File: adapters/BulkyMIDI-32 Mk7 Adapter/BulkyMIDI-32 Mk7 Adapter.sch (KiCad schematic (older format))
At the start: 12 parts, among them J1 Gameport, J2 MIDI OUT, J3 MIDI IN, U1 6N138, U3 74LS00

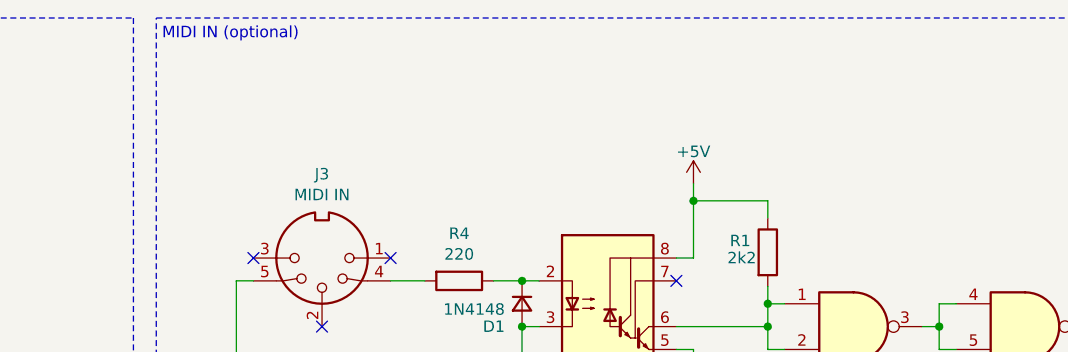
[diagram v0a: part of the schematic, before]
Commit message: Add schematic
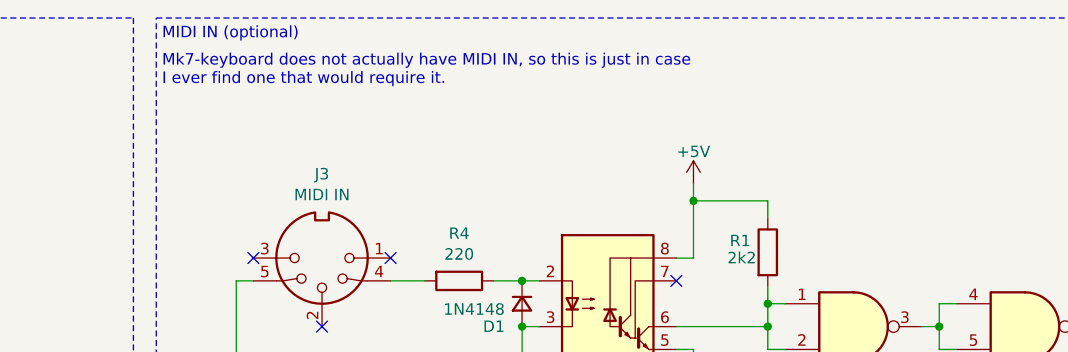
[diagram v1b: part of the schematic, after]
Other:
- note added: "Mk7-keyboard does not actually have MIDI IN, so this is just in case\nI ever find one that would require it."
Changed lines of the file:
@@
 Text Notes 1925 1250 0    50   ~ 0
 Gameport
+Text Notes 5125 1450 0    50   ~ 0
+Mk7-keyboard does not actually have MIDI IN, so this is just in case\nI ever find one that would require it.
 $EndSCHEMATC

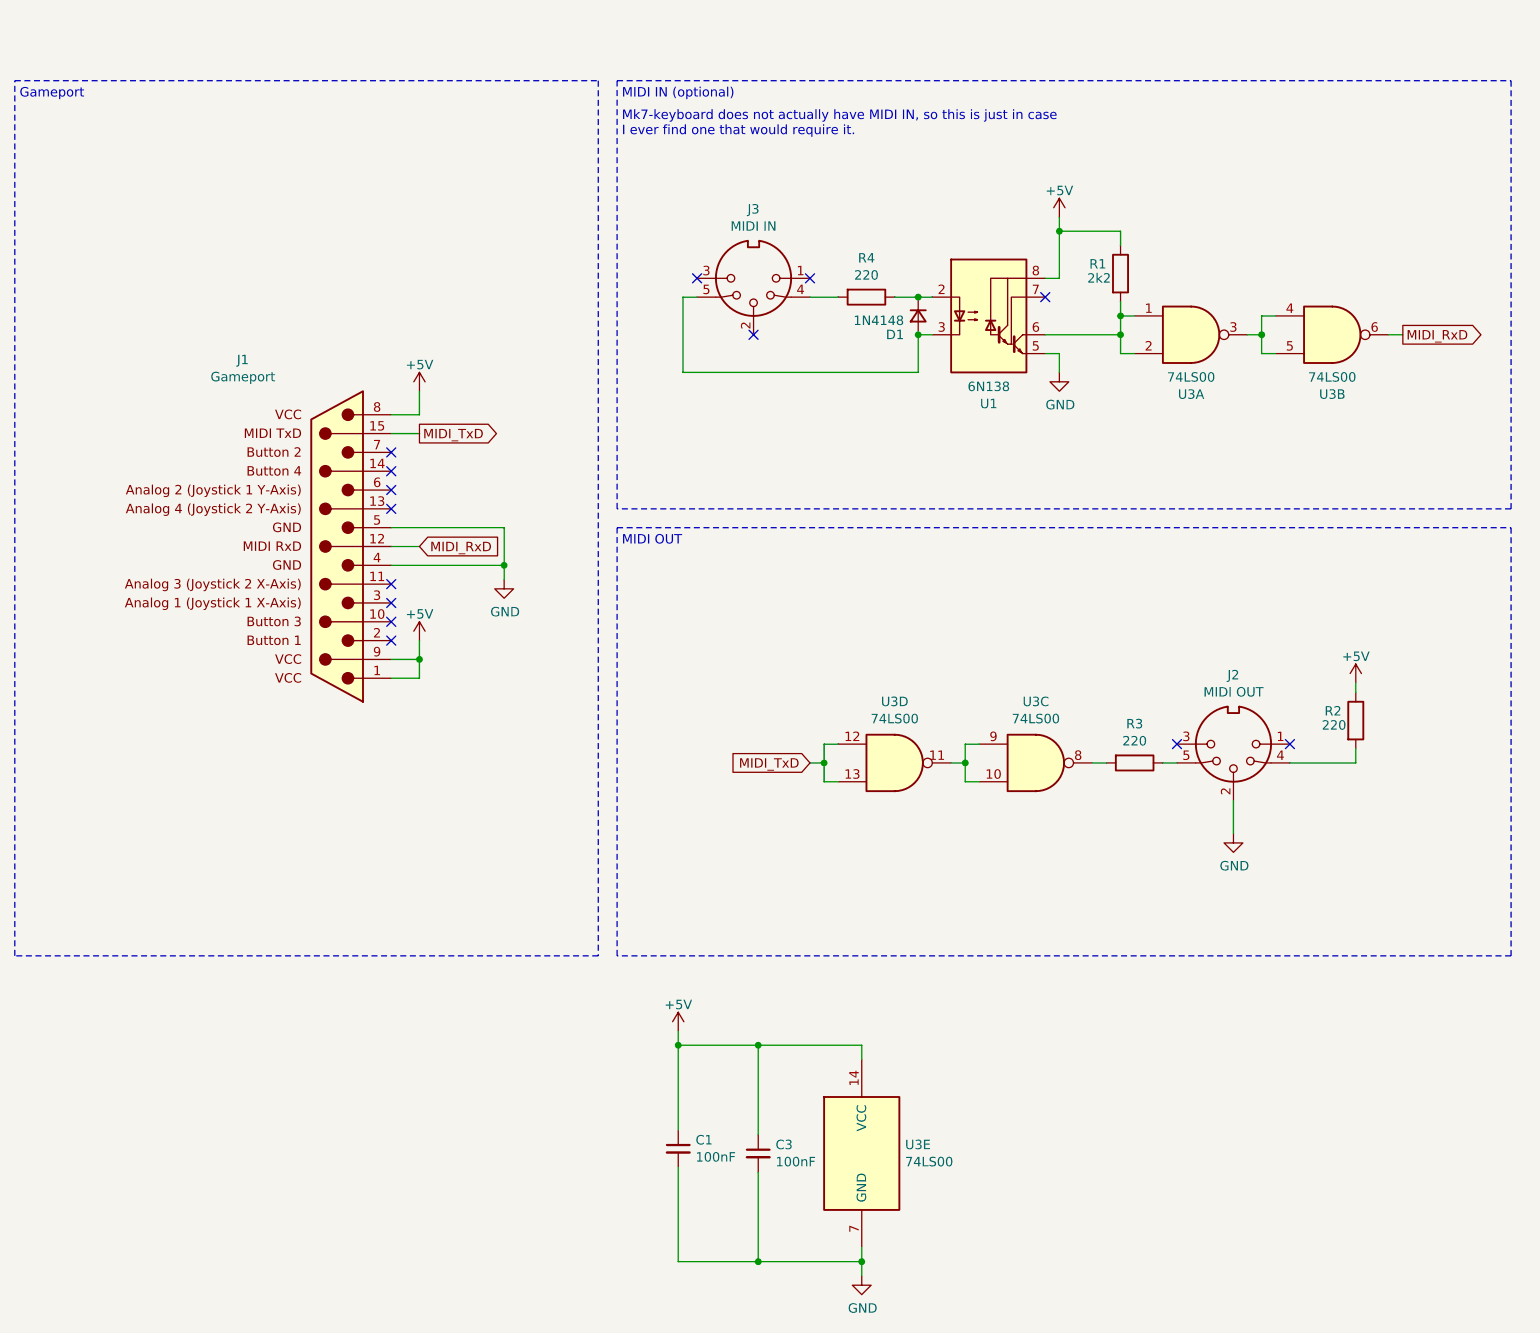
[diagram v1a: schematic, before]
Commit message: Mk7 adapter needs external power
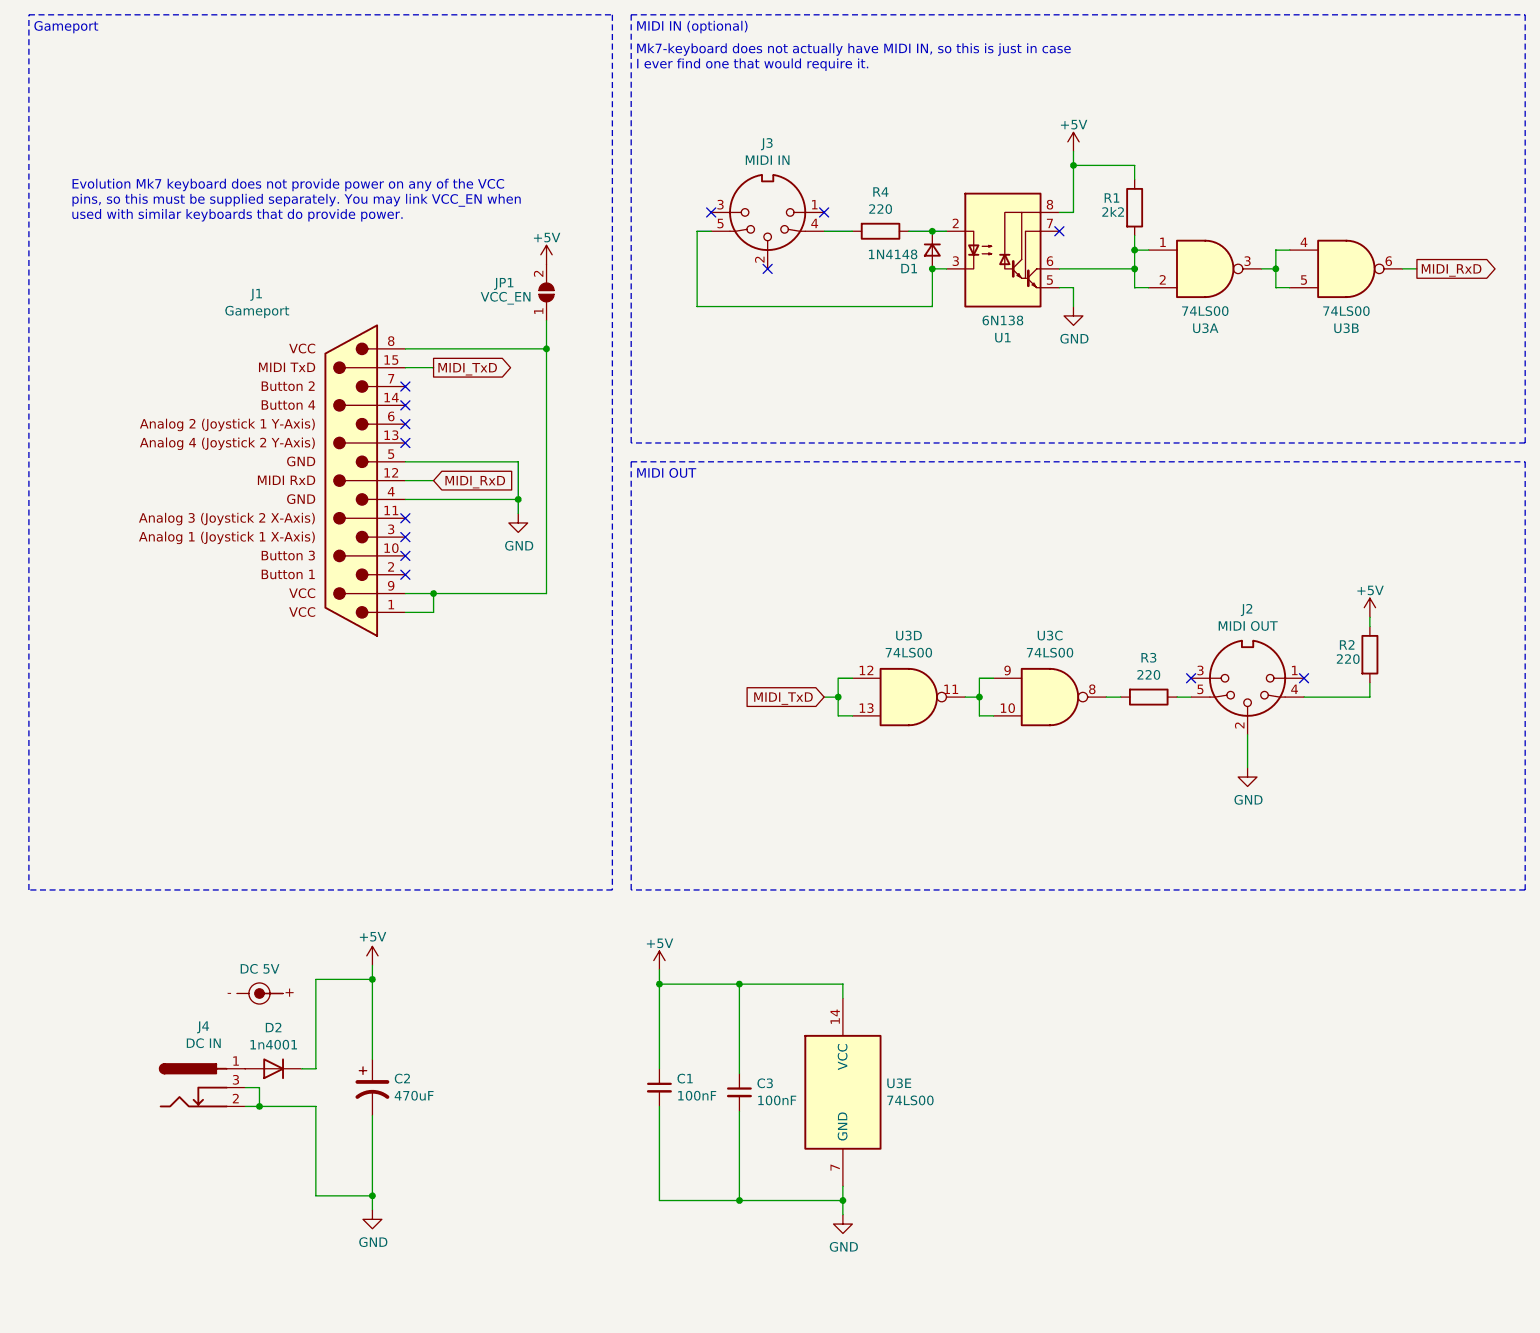
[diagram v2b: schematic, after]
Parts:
- added C2: 470uF, Capacitor_THT:CP_Radial_D8.0mm_P3.50mm, symbol Device:CP1
- added D2: 1n4001, Diode_THT:D_DO-41_SOD81_P10.16mm_Horizontal, symbol Device:D
- added J4: DC IN, BulkyMIDI-32:BARREL_JACK, symbol barrel_jack:barrel_9v
- added JP1: VCC_EN, Jumper:SolderJumper-2_P1.3mm_Open_Pad1.0x1.5mm, symbol Jumper:SolderJumper_2_Open
- added SYM1: DC 5V, BulkyMIDI-32:PWR_Specification, symbol BulkyMIDI:DC_5V
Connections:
- net +5V: now also C2.1, D2.1 (K), JP1.2 (B); no longer J1.1 (VCC), J1.8 (VCC), J1.9 (VCC)
- net GND: now also C2.2, J4.2, J4.3
- new net: D2.2 (A), J4.1
- new net: J1.1 (VCC), J1.8 (VCC), J1.9 (VCC), JP1.1 (A)
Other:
- note added: "Evolution Mk7 keyboard does not provide power on any of the VCC\npins, so this must be supplied separately. You may link VCC_EN when\nused with similar keyboards that do provide power."
- moved on the sheet: C3, J1, R1, R3, U1, U3A, U3B, U3C, U3D, U3E
